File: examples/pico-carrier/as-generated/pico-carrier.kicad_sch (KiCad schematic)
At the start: 16 parts, among them J1 5V IN, J3 GP0-GP15, J4 GP16-GP28, PWR, U1 Pico

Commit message: Put the vias back where the copper moved, and let the fillets vote
The FPGA board came back from its re-route with two unconnected nets and
three dangling ends, and the cause was older than anything this round
added. The router hands back a via for every layer change; six passes
then reshape the copper - snapping to 45s, chamfering, spreading folds,
and now filleting - and none of them move the holes underneath. A joint
that slides a millimetre from its via is two loose ends and one broken
net, and `_unlooped` then swept the via away as orphaned, because it
kept a via only when a track ended on its exact coordinate.

Two fixes, both about what "connected" means. A via lives if kept copper
*touches* it, not if a coordinate matches. And a new `_joined` pass
re-derives the joints from the copper that actually got written: where a
net ends on two layers at one point with no via reaching it, one goes
back in. It reads the finished geometry, so it cannot drift the way six
separate passes carrying vias along with them would.

The same reasoning fixes two rules that had been measuring coordinates
rather than copper. `route.stub` matched a track end to a via's centre
exactly, and called a joint a stub whenever a reshaping pass had moved
it a quarter of a millimetre inside the very barrel it was connected to.
`route.width_step` walked a neck back to its pad and stopped at the
first width change - which, on a filleted board, is the teardrop, so
every escape's neck stopped being recognised as one.

While the three copies of the post-route pipeline were being edited for
the third time this session, they became one function. That is how
`_teardrops` had come to run on two of the three exits.

All five boards: DRC clean on both matrix versions, nothing unconnected.
Four pass their gates; the FPGA board is down to the two-layer bill it
has always had - four nets over plane cuts and one 88 degree corner.

Co-Authored-By: Claude Fable 5 <noreply@anthropic.com>
Claude-Session: https:/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
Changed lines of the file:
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@@
     (exclude_from_sim no) (in_bom no) (on_board yes) (dnp no)
     (property "Reference" "H1" (at 227.64 145.86 0) (effects (font (size 1.27 1.27)) (justify right)))
-    (property "Value" "M3" (at 232.72 152.21 0) (effects (font (size 1.27 1.27)) (justify left)))
+    (property "Value" "M3" (at 232.72 152.21 0) (effects (font (size 1.27 1.27)) (justify left) hide))
     (property "Footprint" "MountingHole:MountingHole_3.2mm_M3" (at 228.91 149.67 0) (effects (font (size 1.27 1.27)) hide))
     (property "Datasheet" "~" (at 228.91 149.67 0) (effects (font (size 1.27 1.27)) hide))
@@
     (exclude_from_sim no) (in_bom no) (on_board yes) (dnp no)
     (property "Reference" "H2" (at 240.34 145.86 0) (effects (font (size 1.27 1.27)) (justify right)))
-    (property "Value" "M3" (at 245.42 152.21 0) (effects (font (size 1.27 1.27)) (justify left)))
+    (property "Value" "M3" (at 245.42 152.21 0) (effects (font (size 1.27 1.27)) (justify left) hide))
     (property "Footprint" "MountingHole:MountingHole_3.2mm_M3" (at 241.61 149.67 0) (effects (font (size 1.27 1.27)) hide))
     (property "Datasheet" "~" (at 241.61 149.67 0) (effects (font (size 1.27 1.27)) hide))
@@
     (exclude_from_sim no) (in_bom no) (on_board yes) (dnp no)
     (property "Reference" "H3" (at 253.04 145.86 0) (effects (font (size 1.27 1.27)) (justify right)))
-    (property "Value" "M3" (at 258.12 152.21 0) (effects (font (size 1.27 1.27)) (justify left)))
+    (property "Value" "M3" (at 258.12 152.21 0) (effects (font (size 1.27 1.27)) (justify left) hide))
     (property "Footprint" "MountingHole:MountingHole_3.2mm_M3" (at 254.31 149.67 0) (effects (font (size 1.27 1.27)) hide))
     (property "Datasheet" "~" (at 254.31 149.67 0) (effects (font (size 1.27 1.27)) hide))
@@
     (exclude_from_sim no) (in_bom no) (on_board yes) (dnp no)
     (property "Reference" "H4" (at 265.74 145.86 0) (effects (font (size 1.27 1.27)) (justify right)))
-    (property "Value" "M3" (at 270.82 152.21 0) (effects (font (size 1.27 1.27)) (justify left)))
+    (property "Value" "M3" (at 270.82 152.21 0) (effects (font (size 1.27 1.27)) (justify left) hide))
     (property "Footprint" "MountingHole:MountingHole_3.2mm_M3" (at 267.01 149.67 0) (effects (font (size 1.27 1.27)) hide))
     (property "Datasheet" "~" (at 267.01 149.67 0) (effects (font (size 1.27 1.27)) hide))
@@
     (exclude_from_sim no) (in_bom no) (on_board yes) (dnp no)
     (property "Reference" "FID1" (at 100.64 145.86 0) (effects (font (size 1.27 1.27)) (justify right)))
-    (property "Value" "Fiducial" (at 105.72 152.21 0) (effects (font (size 1.27 1.27)) (justify left)))
+    (property "Value" "Fiducial" (at 105.72 152.21 0) (effects (font (size 1.27 1.27)) (justify left) hide))
     (property "Footprint" "Fiducial:Fiducial_1mm_Mask2mm" (at 101.91 149.67 0) (effects (font (size 1.27 1.27)) hide))
     (property "Datasheet" "~" (at 101.91 149.67 0) (effects (font (size 1.27 1.27)) hide))
@@
     (exclude_from_sim no) (in_bom no) (on_board yes) (dnp no)
     (property "Reference" "FID2" (at 113.34 145.86 0) (effects (font (size 1.27 1.27)) (justify right)))
-    (property "Value" "Fiducial" (at 118.42 152.21 0) (effects (font (size 1.27 1.27)) (justify left)))
+    (property "Value" "Fiducial" (at 118.42 152.21 0) (effects (font (size 1.27 1.27)) (justify left) hide))
     (property "Footprint" "Fiducial:Fiducial_1mm_Mask2mm" (at 114.61 149.67 0) (effects (font (size 1.27 1.27)) hide))
     (property "Datasheet" "~" (at 114.61 149.67 0) (effects (font (size 1.27 1.27)) hide))
@@
     (exclude_from_sim no) (in_bom no) (on_board yes) (dnp no)
     (property "Reference" "FID3" (at 115.88 145.86 0) (effects (font (size 1.27 1.27)) (justify left)))
-    (property "Value" "Fiducial" (at 105.72 152.21 0) (effects (font (size 1.27 1.27)) (justify right)))
+    (property "Value" "Fiducial" (at 105.72 152.21 0) (effects (font (size 1.27 1.27)) (justify right) hide))
     (property "Footprint" "Fiducial:Fiducial_1mm_Mask2mm" (at 114.61 149.67 0) (effects (font (size 1.27 1.27)) hide))
     (property "Datasheet" "~" (at 114.61 149.67 0) (effects (font (size 1.27 1.27)) hide))

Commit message: Leave room for the screw, and print the ink where the board is
The screw holes were placed against the hole's own courtyard, which is the
drill plus a whisker - so on four of the five boards a hole sat inside a
connector's mating space, closest 0.42 mm. What goes through an M3 hole is a
pan head on a washer, seven millimetres of steel lying flat, and a connector
wants its shell, its wires and the fingers that fit them on top of that. The
spot search now keeps the fastener's own circle clear of every part body and
gives connectors CONNECTOR_ACCESS more, and three rules say so when a board
does not: mechanical.fastener_clearance, mechanical.connector_access and
mechanical.fastener_copper, all blocking for a generated design.

Silk was measured with a per-character advance of 0.78, and KiCad's stroke
font is proportional at 0.94 to 1.07. Everything downstream of that estimate
was placing ink where it did not fit: a legend across a capacitor's land, a
designator through the board's own name. `_text_extent` takes the top of the
measured range, adds the fab's clearance and is used by every silk placement.

Three placements also fell through to a position nobody chose. A designator
that found nothing kept its library offset, which for a part in a corner
points off the board; the board id took the first of eight fixed strips; a
legend took the least bad of six spots. All three are scored now, over
candidate sets wide enough to have an answer - and a pad-less footprint, which
is what a mounting hole is, is no longer skipped outright.

silk.off_board reports the case KiCad's own test cannot: ink that clears the
edge entirely is never printed, and DRC only measures ink that crosses it.

_unspiked redraws a corner tighter than a right angle as the elbow between its
neighbours - one diagonal, one straight, no step back to a heading the line
has already left. It is never longer than what it replaces.

All four fast boards: 0 errors, 0 warnings.

Co-Authored-By: Claude Fable 5 <no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
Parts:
- removed FID3: Fiducial, Fiducial:Fiducial_1mm_Mask2mm, symbol Mechanical:Fiducial
- removed H2, H3, H4: M3, MountingHole:MountingHole_3.2mm_M3, symbol Mechanical:MountingHole
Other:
- moved on the sheet: FID1, H1
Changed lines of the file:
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@@
     (instances (project "pico-carrier" (path "/f86b03a2-2f64-5dc5-a6a7-b575bc25ae3a" (reference "D3") (unit 1))))
   )
-  (symbol (lib_id "Mechanical:MountingHole") (at 228.91 149.67 0.0) (unit 1)
+  (symbol (lib_id "Mechanical:MountingHole") (at 101.91 149.67 0.0) (unit 1)
     (exclude_from_sim no) (in_bom no) (on_board yes) (dnp no)
-    (property "Reference" "H1" (at 227.64 145.86 0) (effects (font (size 1.27 1.27)) (justify right)))
-    (property "Value" "M3" (at 232.72 152.21 0) (effects (font (size 1.27 1.27)) (justify left) hide))
-    (property "Footprint" "MountingHole:MountingHole_3.2mm_M3" (at 228.91 149.67 0) (effects (font (size 1.27 1.27)) hide))
-    (property "Datasheet" "~" (at 228.91 149.67 0) (effects (font (size 1.27 1.27)) hide))
+    (property "Reference" "H1" (at 100.64 145.86 0) (effects (font (size 1.27 1.27)) (justify right)))
+    (property "Value" "M3" (at 105.72 152.21 0) (effects (font (size 1.27 1.27)) (justify left) hide))
+    (property "Footprint" "MountingHole:MountingHole_3.2mm_M3" (at 101.91 149.67 0) (effects (font (size 1.27 1.27)) hide))
+    (property "Datasheet" "~" (at 101.91 149.67 0) (effects (font (size 1.27 1.27)) hide))
     (instances (project "pico-carrier" (path "/f86b03a2-2f64-5dc5-a6a7-b575bc25ae3a" (reference "H1") (unit 1))))
   )
-  (symbol (lib_id "Mechanical:MountingHole") (at 241.61 149.67 0.0) (unit 1)
+  (symbol (lib_id "Mechanical:Fiducial") (at 114.61 149.67 0.0) (unit 1)
     (exclude_from_sim no) (in_bom no) (on_board yes) (dnp no)
-    (property "Reference" "H2" (at 240.34 145.86 0) (effects (font (size 1.27 1.27)) (justify right)))
-    (property "Value" "M3" (at 245.42 152.21 0) (effects (font (size 1.27 1.27)) (justify left) hide))
-    (property "Footprint" "MountingHole:MountingHole_3.2mm_M3" (at 241.61 149.67 0) (effects (font (size 1.27 1.27)) hide))
-    (property "Datasheet" "~" (at 241.61 149.67 0) (effects (font (size 1.27 1.27)) hide))
-    (instances (project "pico-carrier" (path "/f86b03a2-2f64-5dc5-a6a7-b575bc25ae3a" (reference "H2") (unit 1))))
-  )
-  (symbol (lib_id "Mechanical:MountingHole") (at 254.31 149.67 0.0) (unit 1)
-    (exclude_from_sim no) (in_bom no) (on_board yes) (dnp no)
-    (property "Reference" "H3" (at 253.04 145.86 0) (effects (font (size 1.27 1.27)) (justify right)))
-    (property "Value" "M3" (at 258.12 152.21 0) (effects (font (size 1.27 1.27)) (justify left) hide))
-    (property "Footprint" "MountingHole:MountingHole_3.2mm_M3" (at 254.31 149.67 0) (effects (font (size 1.27 1.27)) hide))
-    (property "Datasheet" "~" (at 254.31 149.67 0) (effects (font (size 1.27 1.27)) hide))
-    (instances (project "pico-carrier" (path "/f86b03a2-2f64-5dc5-a6a7-b575bc25ae3a" (reference "H3") (unit 1))))
-  )
-  (symbol (lib_id "Mechanical:MountingHole") (at 267.01 149.67 0.0) (unit 1)
-    (exclude_from_sim no) (in_bom no) (on_board yes) (dnp no)
-    (property "Reference" "H4" (at 265.74 145.86 0) (effects (font (size 1.27 1.27)) (justify right)))
-    (property "Value" "M3" (at 270.82 152.21 0) (effects (font (size 1.27 1.27)) (justify left) hide))
-    (property "Footprint" "MountingHole:MountingHole_3.2mm_M3" (at 267.01 149.67 0) (effects (font (size 1.27 1.27)) hide))
-    (property "Datasheet" "~" (at 267.01 149.67 0) (effects (font (size 1.27 1.27)) hide))
-    (instances (project "pico-carrier" (path "/f86b03a2-2f64-5dc5-a6a7-b575bc25ae3a" (reference "H4") (unit 1))))
-  )
-  (symbol (lib_id "Mechanical:Fiducial") (at 101.91 149.67 0.0) (unit 1)
-    (exclude_from_sim no) (in_bom no) (on_board yes) (dnp no)
-    (property "Reference" "FID1" (at 100.64 145.86 0) (effects (font (size 1.27 1.27)) (justify right)))
-    (property "Value" "Fiducial" (at 105.72 152.21 0) (effects (font (size 1.27 1.27)) (justify left) hide))
-    (property "Footprint" "Fiducial:Fiducial_1mm_Mask2mm" (at 101.91 149.67 0) (effects (font (size 1.27 1.27)) hide))
-    (property "Datasheet" "~" (at 101.91 149.67 0) (effects (font (size 1.27 1.27)) hide))
+    (property "Reference" "FID1" (at 113.34 145.86 0) (effects (font (size 1.27 1.27)) (justify right)))
+    (property "Value" "Fiducial" (at 118.42 152.21 0) (effects (font (size 1.27 1.27)) (justify left) hide))
+    (property "Footprint" "Fiducial:Fiducial_1mm_Mask2mm" (at 114.61 149.67 0) (effects (font (size 1.27 1.27)) hide))
+    (property "Datasheet" "~" (at 114.61 149.67 0) (effects (font (size 1.27 1.27)) hide))
     (instances (project "pico-carrier" (path "/f86b03a2-2f64-5dc5-a6a7-b575bc25ae3a" (reference "FID1") (unit 1))))
   )
   (symbol (lib_id "Mechanical:Fiducial") (at 114.61 149.67 0.0) (unit 1)
     (exclude_from_sim no) (in_bom no) (on_board yes) (dnp no)
-    (property "Reference" "FID2" (at 113.34 145.86 0) (effects (font (size 1.27 1.27)) (justify right)))
-    (property "Value" "Fiducial" (at 118.42 152.21 0) (effects (font (size 1.27 1.27)) (justify left) hide))
+    (property "Reference" "FID2" (at 115.88 145.86 0) (effects (font (size 1.27 1.27)) (justify left)))
+    (property "Value" "Fiducial" (at 105.72 152.21 0) (effects (font (size 1.27 1.27)) (justify right) hide))
     (property "Footprint" "Fiducial:Fiducial_1mm_Mask2mm" (at 114.61 149.67 0) (effects (font (size 1.27 1.27)) hide))
     (property "Datasheet" "~" (at 114.61 149.67 0) (effects (font (size 1.27 1.27)) hide))
     (instances (project "pico-carrier" (path "/f86b03a2-2f64-5dc5-a6a7-b575bc25ae3a" (reference "FID2") (unit 1))))
   )
-  (symbol (lib_id "Mechanical:Fiducial") (at 114.61 149.67 0.0) (unit 1)
-    (exclude_from_sim no) (in_bom no) (on_board yes) (dnp no)
-    (property "Reference" "FID3" (at 115.88 145.86 0) (effects (font (size 1.27 1.27)) (justify left)))
-    (property "Value" "Fiducial" (at 105.72 152.21 0) (effects (font (size 1.27 1.27)) (justify right) hide))
-    (property "Footprint" "Fiducial:Fiducial_1mm_Mask2mm" (at 114.61 149.67 0) (effects (font (size 1.27 1.27)) hide))
-    (property "Datasheet" "~" (at 114.61 149.67 0) (effects (font (size 1.27 1.27)) hide))
-    (instances (project "pico-carrier" (path "/f86b03a2-2f64-5dc5-a6a7-b575bc25ae3a" (reference "FID3") (unit 1))))
-  )
   (wire (pts (xy 72.7 82.36) (xy 80.32 82.36)) (stroke (width 0) (type default)))

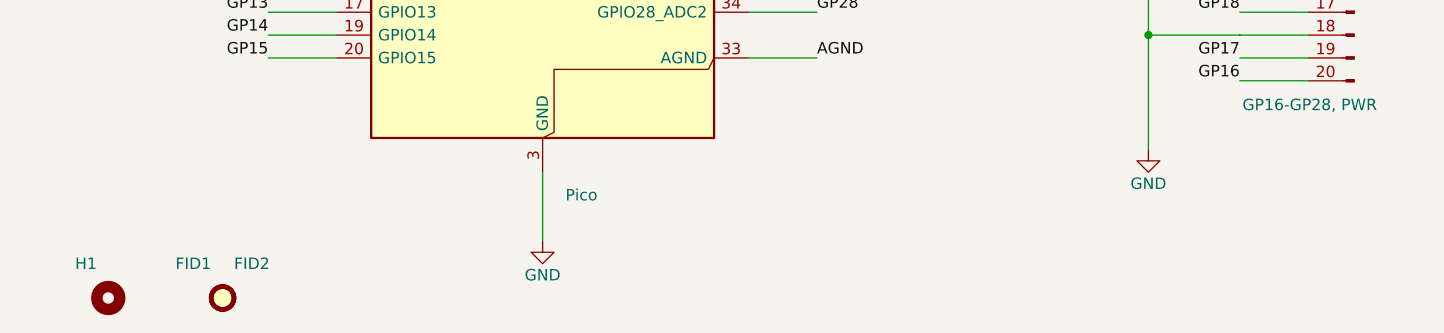
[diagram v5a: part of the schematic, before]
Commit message: Walk the whole edge for a screw hole, and land a joint on its own pad
The fastener clearance was right and the search was not: it slid along two
edges from each corner and gave up, so boards that had had four screw holes
came back with one. It now walks a ring round the board at the inset the
screw needs, taking the nearest free point to each corner - and only from
that corner's own quarter, because a search that asked for the nearest free
point anywhere put three of the four along one edge, each of them the nearest
thing to a different corner. A quarter with no room gives no screw: three
that hold the board flat beat four that hold one side.

A pin header asks for nothing above its courtyard - the socket that fits it
lands inside the outline the header already draws - while a screw terminal's
wires leave horizontally from its face. Treating the two alike is what left a
carrier lined with headers with two holes on one edge. Both the generator and
the rule now tell them apart by footprint.

_landed folds a via that sits beside a plated hole of its own net onto the
hole. The plating already joins the faces, so the via bought nothing and cost
hole-to-hole: two drills a millimetre apart leave 0.15 mm of laminate at a
0.25 mm rule, which is what DRC reported on the opamp board.

The fillets move to the end of the pipeline. A taper is built against the end
of a run, and _landed moves ends, so a teardrop laid before it pointed at
where the run used to stop - a nought-degree corner in the angle rule.

buck-5v, motor-driver, pico-carrier, opamp-filter: 0 errors, 0 warnings.

Co-Authored-By: Claude Fable 5 <noreply@anthropic.com>
Claude-Session: https://claude.ai/code/session_01DUj7Ltu92tWg159mCSacwY
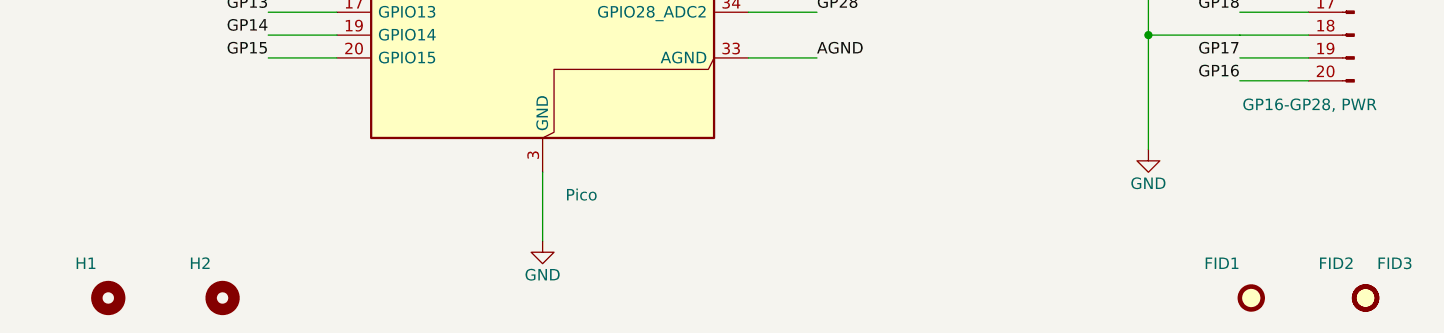
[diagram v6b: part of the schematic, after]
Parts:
- added FID3: Fiducial, Fiducial:Fiducial_1mm_Mask2mm, symbol Mechanical:Fiducial
- added H2: M3, MountingHole:MountingHole_3.2mm_M3, symbol Mechanical:MountingHole
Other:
- moved on the sheet: FID1, FID2
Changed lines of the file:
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@@
     (instances (project "pico-carrier" (path "/f86b03a2-2f64-5dc5-a6a7-b575bc25ae3a" (reference "H1") (unit 1))))
   )
-  (symbol (lib_id "Mechanical:Fiducial") (at 114.61 149.67 0.0) (unit 1)
+  (symbol (lib_id "Mechanical:MountingHole") (at 114.61 149.67 0.0) (unit 1)
     (exclude_from_sim no) (in_bom no) (on_board yes) (dnp no)
-    (property "Reference" "FID1" (at 113.34 145.86 0) (effects (font (size 1.27 1.27)) (justify right)))
-    (property "Value" "Fiducial" (at 118.42 152.21 0) (effects (font (size 1.27 1.27)) (justify left) hide))
-    (property "Footprint" "Fiducial:Fiducial_1mm_Mask2mm" (at 114.61 149.67 0) (effects (font (size 1.27 1.27)) hide))
+    (property "Reference" "H2" (at 113.34 145.86 0) (effects (font (size 1.27 1.27)) (justify right)))
+    (property "Value" "M3" (at 118.42 152.21 0) (effects (font (size 1.27 1.27)) (justify left) hide))
+    (property "Footprint" "MountingHole:MountingHole_3.2mm_M3" (at 114.61 149.67 0) (effects (font (size 1.27 1.27)) hide))
     (property "Datasheet" "~" (at 114.61 149.67 0) (effects (font (size 1.27 1.27)) hide))
+    (instances (project "pico-carrier" (path "/f86b03a2-2f64-5dc5-a6a7-b575bc25ae3a" (reference "H2") (unit 1))))
+  )
+  (symbol (lib_id "Mechanical:Fiducial") (at 228.91 149.67 0.0) (unit 1)
+    (exclude_from_sim no) (in_bom no) (on_board yes) (dnp no)
+    (property "Reference" "FID1" (at 227.64 145.86 0) (effects (font (size 1.27 1.27)) (justify right)))
+    (property "Value" "Fiducial" (at 232.72 152.21 0) (effects (font (size 1.27 1.27)) (justify left) hide))
+    (property "Footprint" "Fiducial:Fiducial_1mm_Mask2mm" (at 228.91 149.67 0) (effects (font (size 1.27 1.27)) hide))
+    (property "Datasheet" "~" (at 228.91 149.67 0) (effects (font (size 1.27 1.27)) hide))
     (instances (project "pico-carrier" (path "/f86b03a2-2f64-5dc5-a6a7-b575bc25ae3a" (reference "FID1") (unit 1))))
   )
-  (symbol (lib_id "Mechanical:Fiducial") (at 114.61 149.67 0.0) (unit 1)
+  (symbol (lib_id "Mechanical:Fiducial") (at 241.61 149.67 0.0) (unit 1)
     (exclude_from_sim no) (in_bom no) (on_board yes) (dnp no)
-    (property "Reference" "FID2" (at 115.88 145.86 0) (effects (font (size 1.27 1.27)) (justify left)))
-    (property "Value" "Fiducial" (at 105.72 152.21 0) (effects (font (size 1.27 1.27)) (justify right) hide))
-    (property "Footprint" "Fiducial:Fiducial_1mm_Mask2mm" (at 114.61 149.67 0) (effects (font (size 1.27 1.27)) hide))
-    (property "Datasheet" "~" (at 114.61 149.67 0) (effects (font (size 1.27 1.27)) hide))
+    (property "Reference" "FID2" (at 240.34 145.86 0) (effects (font (size 1.27 1.27)) (justify right)))
+    (property "Value" "Fiducial" (at 245.42 152.21 0) (effects (font (size 1.27 1.27)) (justify left) hide))
+    (property "Footprint" "Fiducial:Fiducial_1mm_Mask2mm" (at 241.61 149.67 0) (effects (font (size 1.27 1.27)) hide))
+    (property "Datasheet" "~" (at 241.61 149.67 0) (effects (font (size 1.27 1.27)) hide))
     (instances (project "pico-carrier" (path "/f86b03a2-2f64-5dc5-a6a7-b575bc25ae3a" (reference "FID2") (unit 1))))
   )
+  (symbol (lib_id "Mechanical:Fiducial") (at 241.61 149.67 0.0) (unit 1)
+    (exclude_from_sim no) (in_bom no) (on_board yes) (dnp no)
+    (property "Reference" "FID3" (at 242.88 145.86 0) (effects (font (size 1.27 1.27)) (justify left)))
+    (property "Value" "Fiducial" (at 232.72 152.21 0) (effects (font (size 1.27 1.27)) (justify right) hide))
+    (property "Footprint" "Fiducial:Fiducial_1mm_Mask2mm" (at 241.61 149.67 0) (effects (font (size 1.27 1.27)) hide))
+    (property "Datasheet" "~" (at 241.61 149.67 0) (effects (font (size 1.27 1.27)) hide))
+    (instances (project "pico-carrier" (path "/f86b03a2-2f64-5dc5-a6a7-b575bc25ae3a" (reference "FID3") (unit 1))))
+  )
   (wire (pts (xy 72.7 82.36) (xy 80.32 82.36)) (stroke (width 0) (type default)))
